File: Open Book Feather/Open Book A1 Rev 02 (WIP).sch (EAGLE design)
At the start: 114 parts, among them J1 SJ-43514-SMT, J2 10118193-0001LF, Q1 DMG341, Q2 IRLML0100, SW1 SPDT_SWITCH, U1 AP2112-3.3, U2 MCP73831T-2ACI/OT, U3 ATSAMD51J64-TQFP(10X10), U4 GD25Q16C (or GD25Q32C), U5 74AC165D, U6 GD25Q16C (or GD25Q32C), U7 23K256-I/SN, X1 JSTPH, X2 2x5 0.05" SWD

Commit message: added mic preamp
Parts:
- added C32: 0.1µF, microbuilder:CAP_CERAMIC0805-NOOUTLINE
- added C33: 0.01uF, microbuilder:CAP_CERAMIC0805-NOOUTLINE
- added C34: 100pF, microbuilder:CAP_CERAMIC0805-NOOUTLINE
- added C35: 10uF, microbuilder:CAP_CERAMIC0805-NOOUTLINE
- added R10, R11: 1M, microbuilder:RESISTOR0805_NOOUTLINE
- added R12: 100K, microbuilder:RESISTOR0805_NOOUTLINE
- added R13, R23, R24: 1K, microbuilder:RESISTOR0805_NOOUTLINE
- added U8: MAX4466EXK+T, microbuilder:AUDIOAMP_MAX4466
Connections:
- new net A10_MICAMP: C34.1, R12.2, U3G$1.PA07/I7/AIN7/SERCOM0.3, U8.OUT
- new net N$65: C32.1, R13.2, R23.1
- new net N$67: C33.2, R10.2, R11.1, U8.IN+
- new net N$68: C34.2, R12.1, R24.1, U8.IN-
- new net N$69: C35.1, R24.2
- net A7_MIC: now also C33.1, R13.1
- net AGND: now also C32.2, C35.2, R10.1, U8.GND
- net AVCC: now also R11.2, R23.2, U8.VCC
- net SD_CD: no longer U3G$1.PA07/I7/AIN7/SERCOM0.3
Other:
- note added: "+1"
- note added: "= ~25-125x gain"
- note added: "Gain ="
- note added: "Low pass F3db = 1/R5*C4*2pi"
- note added: "R5"
- note added: "VR1+R7"

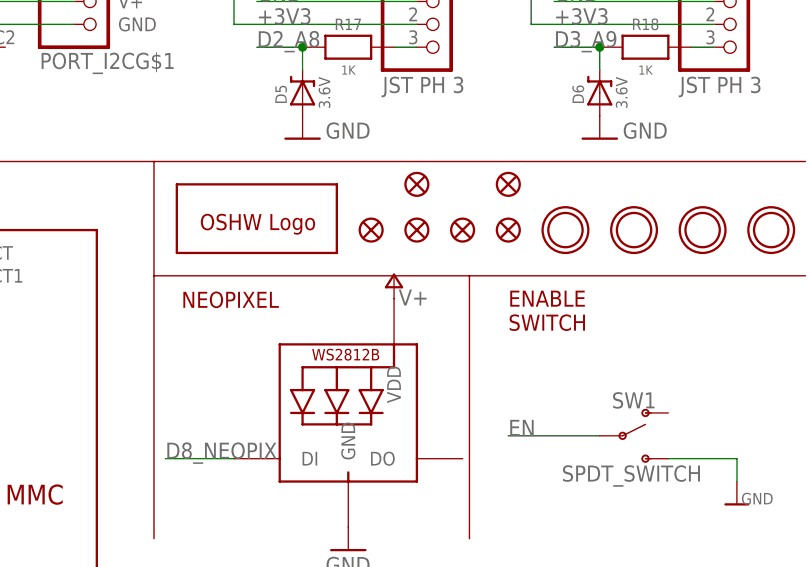
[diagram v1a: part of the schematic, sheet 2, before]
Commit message: rearrange power supply block, power neopixel from regulator
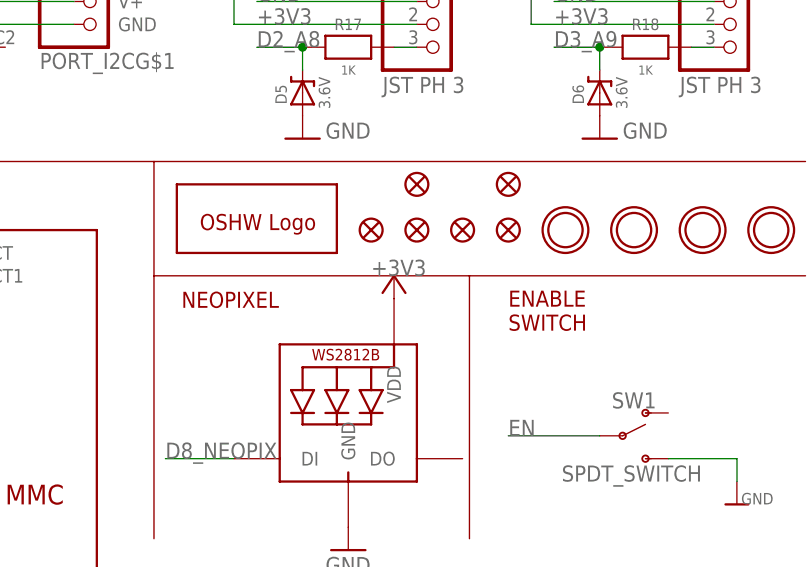
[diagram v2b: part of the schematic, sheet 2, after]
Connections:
- net +3V3: now also STATUS.VDD
- net V+: no longer STATUS.VDD
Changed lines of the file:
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@@
 <grid distance="0.1" unitdist="inch" unit="inch" style="lines" multiple="1" display="no" altdistance="0.01" altunitdist="inch" altunit="inch"/>
 <layers>
-<layer number="1" name="Top" color="4" fill="1" visible="yes" active="no"/>
-<layer number="2" name="Route2" color="1" fill="3" visible="yes" active="no"/>
-<layer number="3" name="Route3" color="4" fill="3" visible="yes" active="no"/>
-<layer number="4" name="Route4" color="1" fill="4" visible="yes" active="no"/>
-<layer number="5" name="Route5" color="4" fill="4" visible="yes" active="no"/>
-<layer number="6" name="Route6" color="1" fill="8" visible="yes" active="no"/>
-<layer number="7" name="Route7" color="4" fill="8" visible="yes" active="no"/>
-<layer number="8" name="Route8" color="1" fill="2" visible="yes" active="no"/>
-<layer number="9" name="Route9" color="4" fill="2" visible="yes" active="no"/>
-<layer number="10" name="Route10" color="1" fill="7" visible="yes" active="no"/>
-<layer number="11" name="Route11" color="4" fill="7" visible="yes" active="no"/>
-<layer number="12" name="Route12" color="1" fill="5" visible="yes" active="no"/>
-<layer number="13" name="Route13" color="4" fill="5" visible="yes" active="no"/>
-<layer number="14" name="Route14" color="1" fill="6" visible="yes" active="no"/>
-<layer number="15" name="Route15" color="4" fill="6" visible="yes" active="no"/>
-<layer number="16" name="Bottom" color="1" fill="1" visible="yes" active="no"/>
-<layer number="17" name="Pads" color="2" fill="1" visible="yes" active="no"/>
-<layer number="18" name="Vias" color="2" fill="1" visible="yes" active="no"/>
-<layer number="19" name="Unrouted" color="6" fill="1" visible="yes" active="no"/>
-<layer number="20" name="Dimension" color="15" fill="1" visible="yes" active="no"/>
-<layer number="21" name="tPlace" color="14" fill="1" visible="yes" active="no"/>
-<layer number="22" name="bPlace" color="13" fill="1" visible="yes" active="no"/>
-<layer number="23" name="tOrigins" color="15" fill="1" visible="yes" active="no"/>
-<layer number="24" name="bOrigins" color="15" fill="1" visible="yes" active="no"/>
-<layer number="25" name="tNames" color="7" fill="1" visible="yes" active="no"/>
-<layer number="26" name="bNames" color="7" fill="1" visible="yes" active="no"/>
-<layer number="27" name="tValues" color="7" fill="1" visible="yes" active="no"/>
-<layer number="28" name="bValues" color="7" fill="1" visible="yes" active="no"/>
+<layer number="1" name="Top" color="4" fill="1" visible="no" active="no"/>
+<layer number="2" name="Route2" color="1" fill="3" visible="no" active="no"/>
+<layer number="3" name="Route3" color="4" fill="3" visible="no" active="no"/>
+<layer number="4" name="Route4" color="1" fill="4" visible="no" active="no"/>
+<layer number="5" name="Route5" color="4" fill="4" visible="no" active="no"/>
+<layer number="6" name="Route6" color="1" fill="8" visible="no" active="no"/>
+<layer number="7" name="Route7" color="4" fill="8" visible="no" active="no"/>
+<layer number="8" name="Route8" color="1" fill="2" visible="no" active="no"/>
+<layer number="9" name="Route9" color="4" fill="2" visible="no" active="no"/>
+<layer number="10" name="Route10" color="1" fill="7" visible="no" active="no"/>
+<layer number="11" name="Route11" color="4" fill="7" visible="no" active="no"/>
+<layer number="12" name="Route12" color="1" fill="5" visible="no" active="no"/>
+<layer number="13" name="Route13" color="4" fill="5" visible="no" active="no"/>
+<layer number="14" name="Route14" color="1" fill="6" visible="no" active="no"/>
+<layer number="15" name="Route15" color="4" fill="6" visible="no" active="no"/>
+<layer number="16" name="Bottom" color="1" fill="1" visible="no" active="no"/>
+<layer number="17" name="Pads" color="2" fill="1" visible="no" active="no"/>
+<layer number="18" name="Vias" color="2" fill="1" visible="no" active="no"/>
+<layer number="19" name="Unrouted" color="6" fill="1" visible="no" active="no"/>
+<layer number="20" name="Dimension" color="15" fill="1" visible="no" active="no"/>
+<layer number="21" name="tPlace" color="14" fill="1" visible="no" active="no"/>
+<layer number="22" name="bPlace" color="13" fill="1" visible="no" active="no"/>
+<layer number="23" name="tOrigins" color="15" fill="1" visible="no" active="no"/>
+<layer number="24" name="bOrigins" color="15" fill="1" visible="no" active="no"/>
+<layer number="25" name="tNames" color="7" fill="1" visible="no" active="no"/>
+<layer number="26" name="bNames" color="7" fill="1" visible="no" active="no"/>
+<layer number="27" name="tValues" color="7" fill="1" visible="no" active="no"/>
+<layer number="28" name="bValues" color="7" fill="1" visible="no" active="no"/>
 <layer number="29" name="tStop" color="7" fill="3" visible="no" active="no"/>
 <layer number="30" name="bStop" color="7" fill="6" visible="no" active="no"/>
@@
 <layer number="35" name="tGlue" color="7" fill="4" visible="no" active="no"/>
 <layer number="36" name="bGlue" color="7" fill="5" visible="no" active="no"/>
-<layer number="37" name="tTest" color="7" fill="1" visible="yes" active="no"/>
-<layer number="38" name="bTest" color="7" fill="1" visible="yes" active="no"/>
+<layer number="37" name="tTest" color="7" fill="1" visible="no" active="no"/>
+<layer number="38" name="bTest" color="7" fill="1" visible="no" active="no"/>
 <layer number="39" name="tKeepout" color="4" fill="11" visible="no" active="no"/>
 <layer number="40" name="bKeepout" color="1" fill="11" visible="no" active="no"/>
@@
 <layer number="44" name="Drills" color="7" fill="1" visible="no" active="no"/>
 <layer number="45" name="Holes" color="7" fill="1" visible="no" active="no"/>
-<layer number="46" name="Milling" color="3" fill="1" visible="yes" active="no"/>
-<layer number="47" name="Measures" color="7" fill="1" visible="yes" active="no"/>
-<layer number="48" name="Document" color="7" fill="1" visible="yes" active="no"/>
-<layer number="49" name="Reference" color="7" fill="1" visible="yes" active="no"/>
-<layer number="50" name="dxf" color="7" fill="1" visible="yes" active="no"/>
-<layer number="51" name="tDocu" color="7" fill="1" visible="yes" active="no"/>
-<layer number="52" name="bDocu" color="7" fill="1" visible="yes" active="no"/>
-<layer number="53" name="tGND_GNDA" color="7" fill="9" visible="yes" active="no"/>
-<layer number="54" name="bGND_GNDA" color="1" fill="9" visible="yes" active="no"/>
-<layer number="56" name="wert" color="7" fill="1" visible="yes" active="no"/>
-<layer number="57" name="tCAD" color="7" fill="1" visible="yes" active="no"/>
-<layer number="59" name="tCarbon" color="7" fill="1" visible="yes" active="no"/>
-<layer number="60" name="bCarbon" color="7" fill="1" visible="yes" active="no"/>
+<layer number="46" name="Milling" color="3" fill="1" visible="no" active="no"/>
+<layer number="47" name="Measures" color="7" fill="1" visible="no" active="no"/>
+<layer number="48" name="Document" color="7" fill="1" visible="no" active="no"/>
+<layer number="49" name="Reference" color="7" fill="1" visible="no" active="no"/>
+<layer number="50" name="dxf" color="7" fill="1" visible="no" active="no"/>
+<layer number="51" name="tDocu" color="7" fill="1" visible="no" active="no"/>
+<layer number="52" name="bDocu" color="7" fill="1" visible="no" active="no"/>
+<layer number="53" name="tGND_GNDA" color="7" fill="9" visible="no" active="no"/>
+<layer number="54" name="bGND_GNDA" color="1" fill="9" visible="no" active="no"/>
+<layer number="56" name="wert" color="7" fill="1" visible="no" active="no"/>
+<layer number="57" name="tCAD" color="7" fill="1" visible="no" active="no"/>
+<layer number="59" name="tCarbon" color="7" fill="1" visible="no" active="no"/>
+<layer number="60" name="bCarbon" color="7" fill="1" visible="no" active="no"/>
 <layer number="88" name="SimResults" color="9" fill="1" visible="yes" active="yes"/>
 <layer number="89" name="SimProbes" color="9" fill="1" visible="yes" active="yes"/>
@@
 <part name="STATUS" library="adafruit" deviceset="WS2812B" device="3535" value="WS2812B3535"/>
 <part name="P+1" library="supply1" library_urn="urn:adsk.eagle:library:371" deviceset="V+" device=""/>
-<part name="P+2" library="supply1" library_urn="urn:adsk.eagle:library:371" deviceset="V+" device=""/>
 <part name="MS1" library="pygamer-microbuilder" deviceset="FEATHERWING" device="_SMTDUAL"/>
 <part name="U$23" library="My Stuff" deviceset="SPST_TACTILE_SWITCH" device="THRU-SECONDTRY"/>
@@
 <part name="R24" library="microbuilder" deviceset="RESISTOR" device="0805_NOOUTLINE" value="1K"/>
 <part name="FRAME3" library="My Stuff" deviceset="A4L-LOC" device=""/>
+<part name="+3V9" library="supply1" library_urn="urn:adsk.eagle:library:371" deviceset="+3V3" device=""/>
 </parts>
 <sheets>
@@
 </instance>
 <instance part="STATUS" gate="G$1" x="205.74" y="35.56" smashed="yes"/>
-<instance part="P+2" gate="1" x="210.82" y="53.34" smashed="yes">
-<attribute name="VALUE" x="211.328" y="50.038" size="1.778" layer="96"/>
-</instance>
 <instance part="U$23" gate="G$1" x="236.22" y="162.56" smashed="yes">
 <attribute name="NAME" x="233.68" y="166.116" size="1.27" layer="95"/>
@@
 <attribute name="VALUE" x="233.68" y="122.174" size="1.27" layer="96"/>
 </instance>
+<instance part="+3V9" gate="G$1" x="210.82" y="53.34" smashed="yes">
+<attribute name="VALUE" x="208.28" y="53.34" size="1.778" layer="96"/>
+</instance>
 </instances>
 <busses>
@@
 <pinref part="+3V18" gate="G$1" pin="+3V3"/>
 </segment>
+<segment>
+<pinref part="STATUS" gate="G$1" pin="VDD"/>
+<pinref part="+3V9" gate="G$1" pin="+3V3"/>
+</segment>
 </net>
 <net name="GDR" class="0">
@@
 </segment>
 </net>
-<net name="V+" class="1">
-<segment>
-<pinref part="P+2" gate="1" pin="V+"/>
-<pinref part="STATUS" gate="G$1" pin="VDD"/>
-</segment>
-</net>

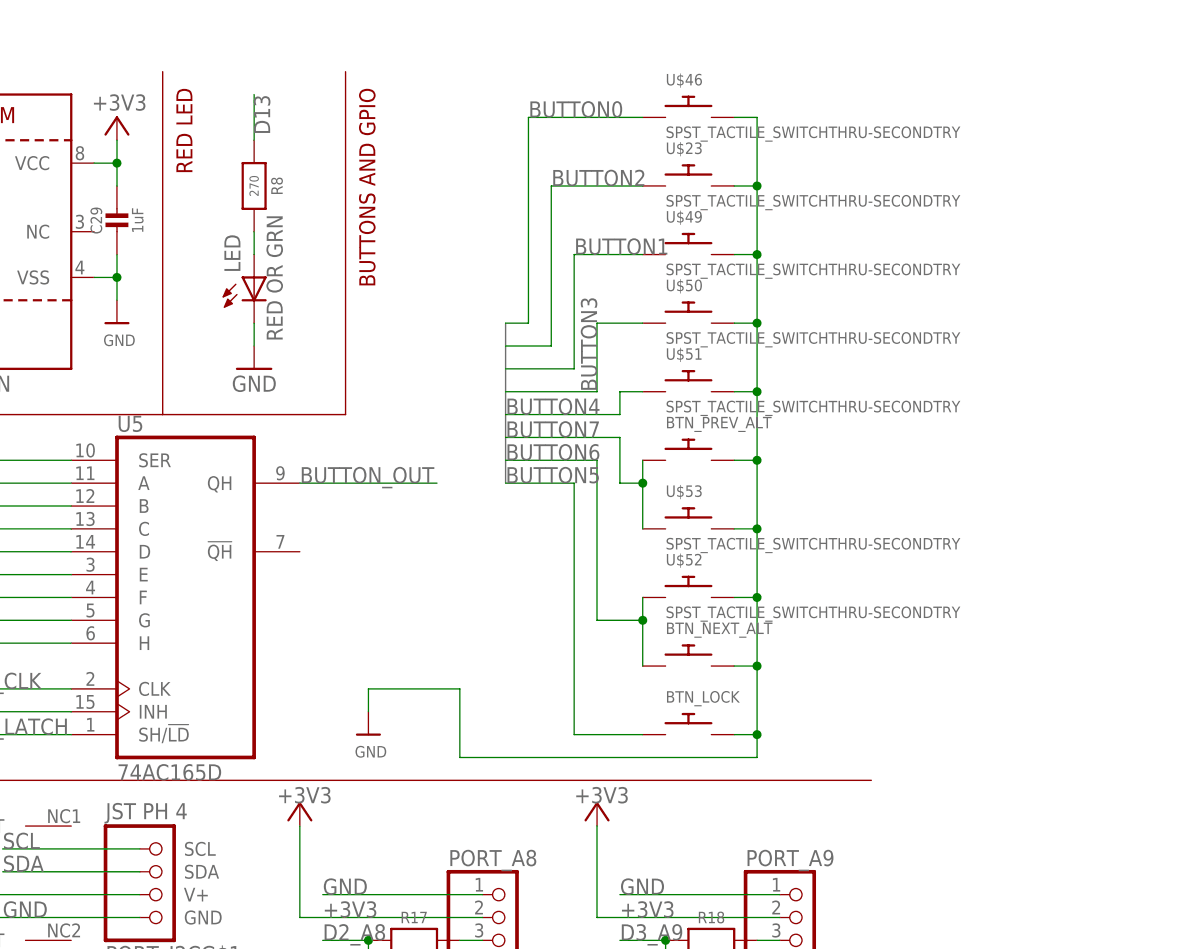
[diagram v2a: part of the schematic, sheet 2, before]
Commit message: fix buttons, add pulldown resistors & remove lock btn from shift reg
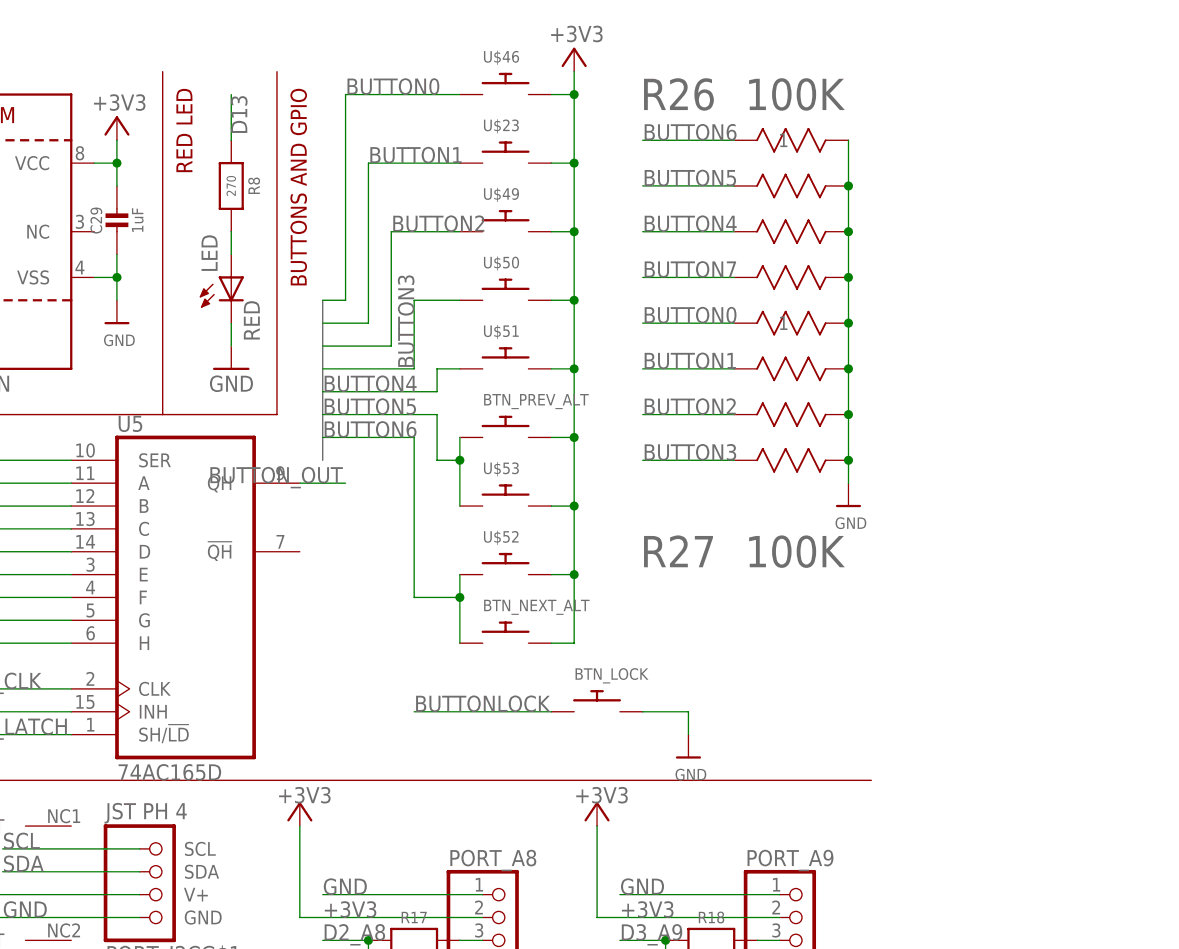
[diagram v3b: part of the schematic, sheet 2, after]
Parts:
- added R26, R27: 100K, resistor array:EXB-V8V103JV
- LED: value RED OR GRN -> RED
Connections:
- new net BUTTONLOCK: BTN_LOCK.P$1, U3G$1.PA27/I11
- net +3V3: now also BTN_NEXT_ALT.P$2, BTN_PREV_ALT.P$2, U$23.P$2, U$46.P$2, U$49.P$2, U$50.P$2, U$51.P$2, U$52.P$2, U$53.P$2
- net BUTTON0: now also R27.1
- net BUTTON1: now also R27.2, U$23.P$1; no longer U$49.P$1
- net BUTTON2: now also R27.3, U$49.P$1; no longer U$23.P$1
- net BUTTON3: now also R27.4
- net BUTTON4: now also R26.3
- net BUTTON5: now also BTN_PREV_ALT.P$1, R26.2, U$53.P$1; no longer BTN_LOCK.P$1, U3G$1.PA27/I11
- net BUTTON6: now also R26.1
- net BUTTON7: now also R26.4; no longer BTN_PREV_ALT.P$1, U$53.P$1
- net GND: now also R26.5, R26.6, R26.7, R26.8, R27.5, R27.6, R27.7, R27.8; no longer BTN_NEXT_ALT.P$2, BTN_PREV_ALT.P$2, U$23.P$2, U$46.P$2, U$49.P$2, U$50.P$2, U$51.P$2, U$52.P$2, U$53.P$2
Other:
- moved on the sheet: BTN_LOCK, BTN_NEXT_ALT, BTN_PREV_ALT, LED, R8, U$23, U$46, U$49, U$50, U$51, U$52, U$53

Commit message: put sd card detect signal on shift register
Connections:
- removed net SD_CD: MICROSD.CARD_DETECT1
- net +3V3: now also R26.5
- net BUTTON7: now also MICROSD.CARD_DETECT1
- net GND: no longer R26.5
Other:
- note added: "This looks ridic but BUTTON7 is now the SD Card Detect line, and it needs a pull-up rather than a pulldown."
